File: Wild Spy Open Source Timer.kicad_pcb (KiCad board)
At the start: 2 copper layers, 30 x 31.3 mm, 16 parts, among them Q2 AO3415, Q3 AO3415, Q4 AO3415, Q5 AO3415

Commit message: PCB components placed
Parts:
- added Breakout1: CONN_02X04, MC_Footprint:4x2connnector_small, F.Cu at (212.1, 121.9)
- added C1: 0.1uF, Capacitors_SMD:C_0603_HandSoldering, B.Cu at (213.4, 104.8)
- added C2: 0.1uF, Capacitors_SMD:C_0603_HandSoldering, B.Cu at (197.5, 109.2)
- added C3: 0.1uF, Capacitors_SMD:C_0603_HandSoldering, B.Cu at (208.9, 119.4)
- added C4: 0.1uF, Capacitors_SMD:C_0603_HandSoldering, B.Cu at (199.4, 117.8)
- added C5: CL10A105KB8NNNC, Capacitors_SMD:C_0805, F.Cu at (199.3, 119.1)
- added C6: 1uF, Capacitors_SMD:C_0603_HandSoldering, B.Cu at (199.4, 121.6)
- added C8: CL10B225KQ8NFNC, Capacitors_SMD:C_0603, F.Cu at (191.1, 118.9)
- added D1: LED, LEDs:LED_0603, F.Cu at (212.7, 116.8)
- added JP1: JUMPER3, jumper:SOLDER-JUMPER_2-WAY, F.Cu at (194.9, 123.8)
- added PBus1: CONN_01X04, Pin_Headers:Pin_Header_Straight_1x04_Pitch2.54mm, F.Cu at (200.7, 97.2)
- added Q1: AO3415, MC_Footprint:SOT-23-HandSoldering, B.Cu at (195.6, 115.3)
- added Q6: AO3415, MC_Footprint:SOT-23-HandSoldering, B.Cu at (191.7, 118.8)
- added R1: 10k, Resistors_SMD:R_0603_HandSoldering, B.Cu at (208.3, 113.7)
- added R10: 3.3k, Resistors_SMD:R_0603_HandSoldering, F.Cu at (204.0, 120.7)
- added R11: 1k, Resistors_SMD:R_0603_HandSoldering, F.Cu at (212.7, 114.9)
- added R2: 10k, Resistors_SMD:R_0603_HandSoldering, B.Cu at (208.3, 115.6)
- added R3: 150k, Resistors_SMD:R_0603_HandSoldering, B.Cu at (196.4, 119.7)
- added R8: 10k, Resistors_SMD:R_0603_HandSoldering, B.Cu at (196.4, 117.8)
- added R9: 1.7k, Resistors_SMD:R_0603_HandSoldering, F.Cu at (204.0, 118.7)
- added SWD1: CONN_01X05, MC_Footprint:SWD_PROG_HEADER, F.Cu at (217.2, 120.0)
- added U1: DS3232SN, Housings_SOIC:SOIC-20W_7.5x12.8mm_Pitch1.27mm, B.Cu at (204.5, 106.0)
- added U2: TPS70933DBVR, TO_SOT_Packages_SMD:SOT-23-5_HandSoldering, F.Cu at (194.9, 118.8)
- added U3: UM6K33N, MC_Footprint:SC88(SOT363), F.Cu at (200.0, 104.8)
- added U4: UM6K33N, MC_Footprint:SC88(SOT363), F.Cu at (208.9, 104.8)
- added U5: ATSAMD21E18B, Housings_DFN_QFN:QFN-32-1EP_5x5mm_Pitch0.5mm, B.Cu at (204.1, 120.4)
- Q2, Q3, Q4, Q5: footprint TO_SOT_Packages_SMD:SOT-23 -> MC_Footprint:SOT-23-HandSoldering
- R4, R5, R6, R7: value 10k -> 100k
- moved Battery1 84.9 mm to (191.1, 122.6)
- moved CH3 66.6 mm to (191.1, 106.7)
- moved Q3 65.6 mm to (194.6, 108.6), turned to 270 degrees
- moved CH2 64.6 mm to (217.0, 97.8)
- moved Q4 60.4 mm to (213.4, 101.0)
- moved Q2 60.0 mm to (195.6, 101.0)
- moved R5 59.1 mm to (195.1, 105.4), turned to 180 degrees
- moved R6 56.9 mm to (213.4, 97.8), turned to 180 degrees
- moved CH1 56.9 mm to (191.1, 97.8)
- moved R4 54.5 mm to (195.6, 97.8), turned to 180 degrees
- moved Q5 50.3 mm to (213.4, 109.9), turned to 270 degrees
- moved CH4 48.1 mm to (217.2, 106.7)
- moved R7 43.3 mm to (213.4, 106.7), turned to 180 degrees
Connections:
- Battery1 pad 1: VAA -> /BAT+
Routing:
- net (no net): track 176.4 -> 6.88 mm, vias 6 -> 0
- net VCC: track 0.00 -> 12.0 mm
- net Net-(Q2-Pad1): track 13.0 -> 1.94 mm, vias 1 -> 0
- net +5V: track 0.00 -> 10.1 mm
- net Net-(Q3-Pad1): track 10.5 -> 2.04 mm, vias 1 -> 0
- net VAA: track 0.00 -> 8.42 mm
- net Net-(Q4-Pad1): track 10.3 -> 1.94 mm, vias 1 -> 0
- net /D+: track 0.00 -> 5.27 mm, vias 0 -> 1
- net /BAT+: track 0.00 -> 4.38 mm
- net Net-(CH2-Pad1): track 8.68 -> 4.47 mm
- net Net-(CH4-Pad1): track 8.54 -> 4.68 mm
- net Net-(Q5-Pad1): track 5.70 -> 1.97 mm
- net /D-: track 0.00 -> 3.18 mm, vias 0 -> 1
- net Net-(C6-Pad2): track 0.00 -> 2.47 mm
- net Net-(C2-Pad2): track 0.00 -> 2.42 mm
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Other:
- net class Default: clearance 0.1524 -> 0.2032; trace_width 0.1524 -> 0.2032
- rule trace_clearance: 0.1524 -> 0.2032

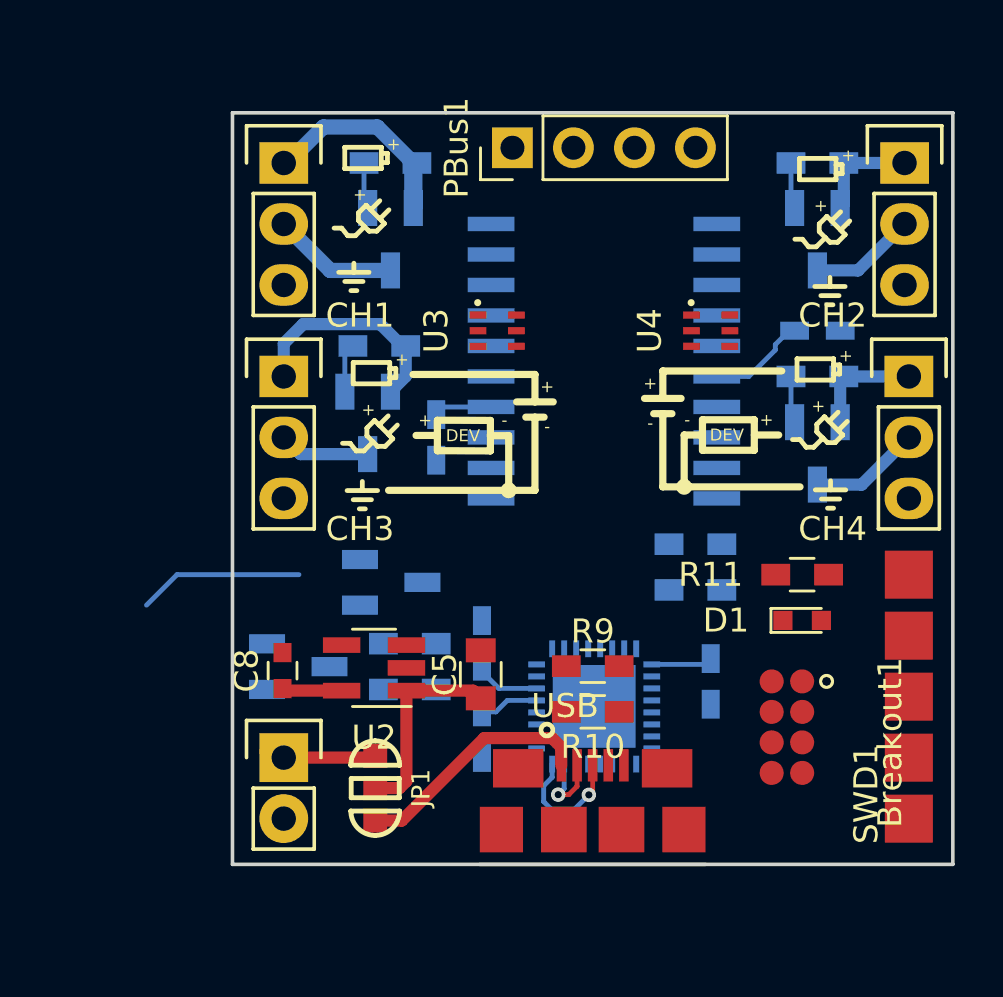
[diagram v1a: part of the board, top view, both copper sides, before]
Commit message: Routing for the Timer PCB- almost done
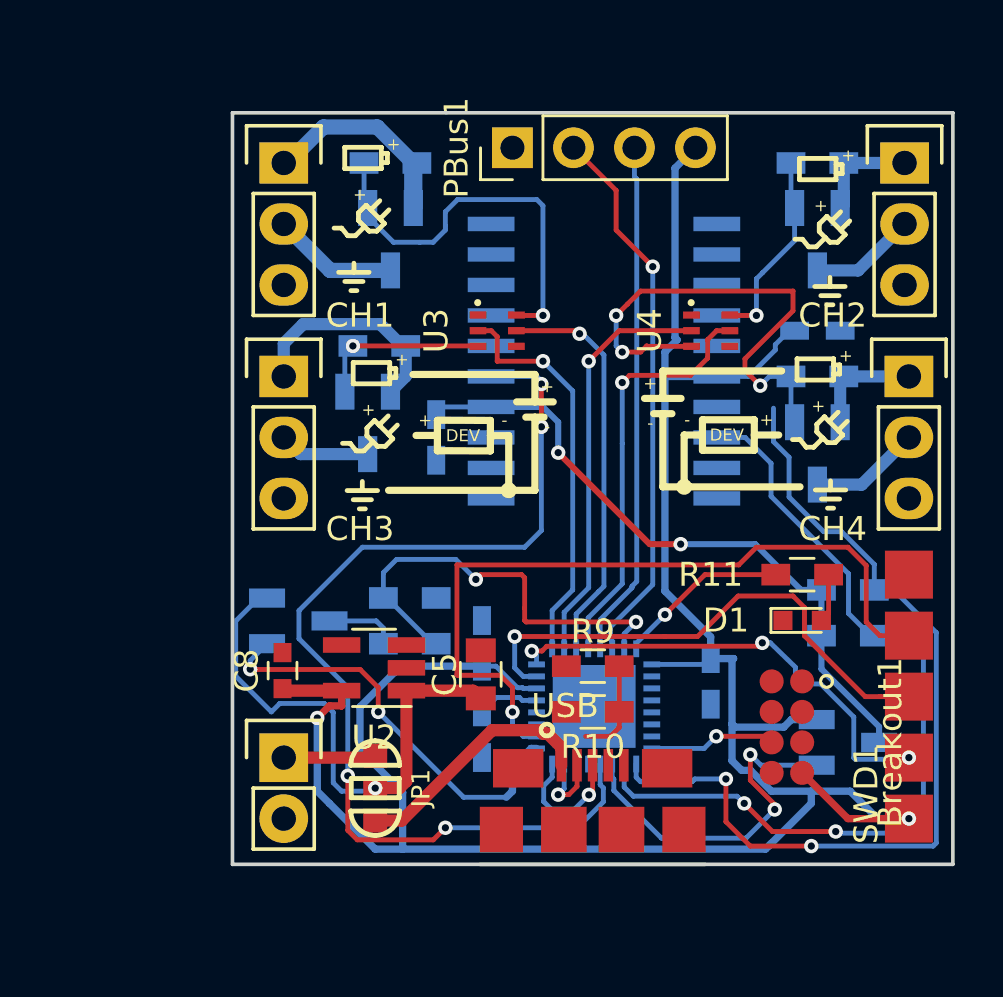
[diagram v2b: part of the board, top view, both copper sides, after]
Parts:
- moved Q1 20.2 mm to (214.6, 121.9)
- moved R2 6.63 mm to (214.6, 117.5)
- moved R1 6.63 mm to (214.6, 115.6)
- moved Q6 1.91 mm to (191.7, 116.9)
- moved R3 1.91 mm to (196.4, 117.8)
- moved R8 1.91 mm to (196.4, 115.9)
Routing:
- net VCC: track 12.0 -> 100.3 mm, vias 0 -> 2
- net /RTC_~INT: track 0.00 -> 43.0 mm, vias 0 -> 4
- net /SDA: track 0.00 -> 37.7 mm, vias 0 -> 2
- net /SCL: track 0.00 -> 35.9 mm, vias 0 -> 2
- net /NRESET: track 0.00 -> 31.9 mm, vias 0 -> 1
- net Net-(C2-Pad2): track 2.42 -> 27.4 mm, vias 0 -> 2
- net /PBus1_MRX: track 0.00 -> 23.0 mm, vias 0 -> 1
- net /SWDCLK: track 0.00 -> 21.9 mm, vias 0 -> 1
- net /PBus1_MTX: track 0.00 -> 21.5 mm
- net /SWDIO: track 0.00 -> 19.8 mm, vias 0 -> 3
- net Net-(Q5-Pad1): track 1.97 -> 20.8 mm, vias 0 -> 3
- net /VBat/15: track 0.00 -> 18.4 mm, vias 0 -> 2
- net /~BatMeasureEn: track 0.00 -> 17.5 mm, vias 0 -> 2
- net /CH4_EN: track 0.00 -> 17.5 mm, vias 0 -> 1
- net /CH2_EN: track 0.00 -> 17.3 mm, vias 0 -> 1
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
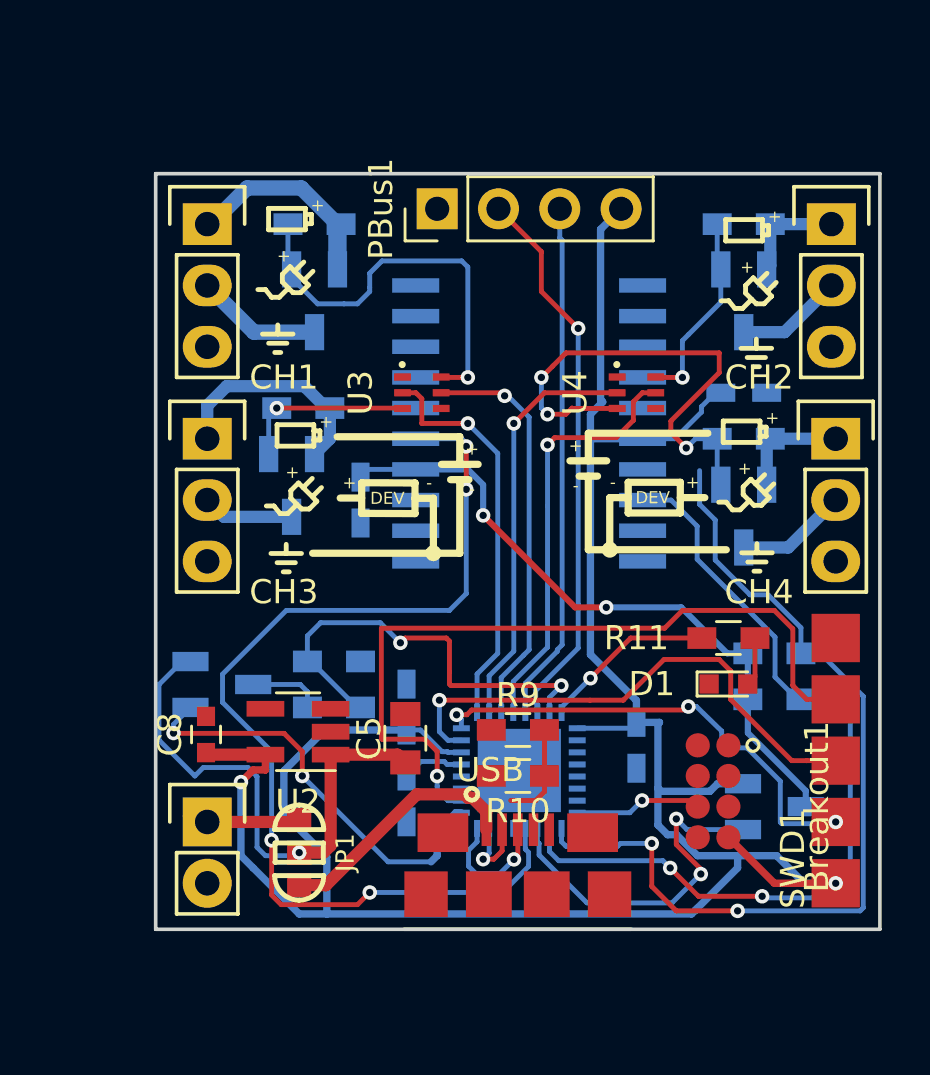
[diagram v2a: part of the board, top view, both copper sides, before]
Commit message: Cleaned up routing on PCB a bit. Made some changes to schematic, added a few things.
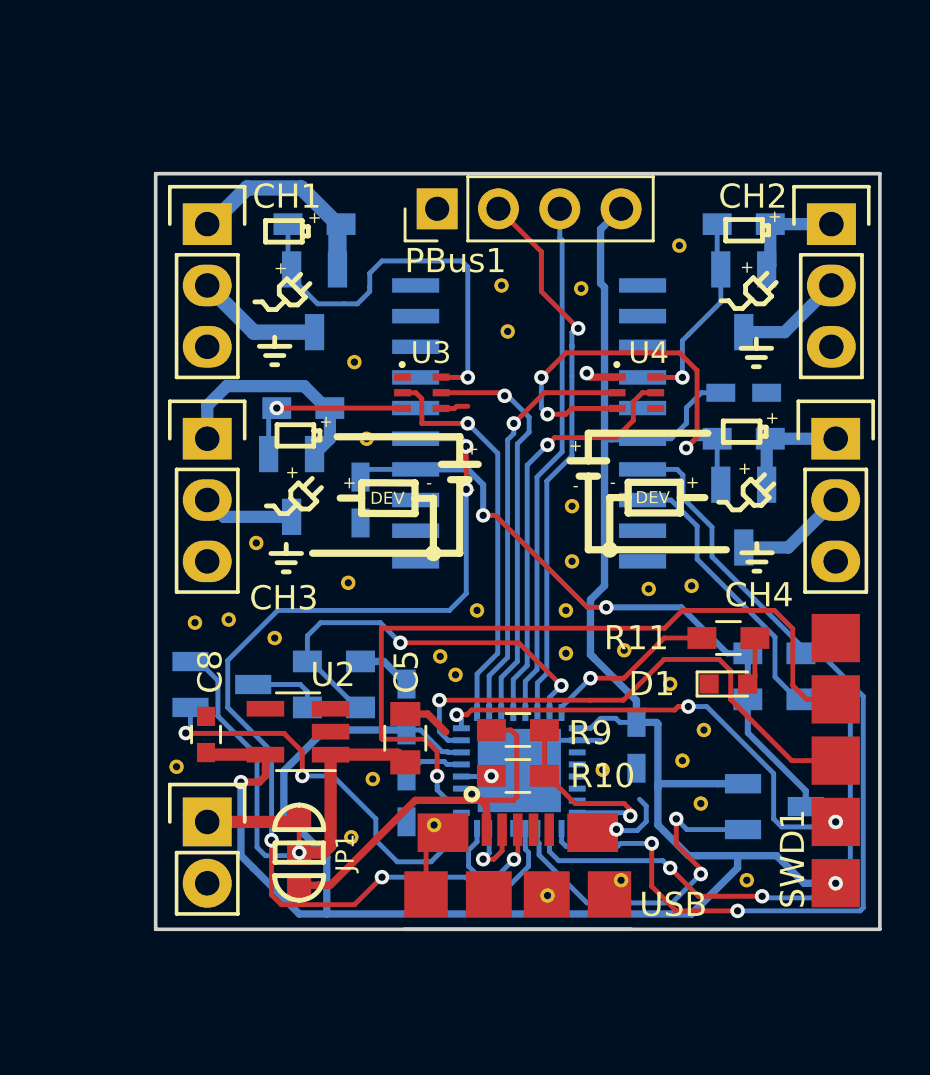
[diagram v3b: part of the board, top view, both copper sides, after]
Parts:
- removed Breakout1: CONN_02X04, MC_Footprint:4x2connnector_small
- added REF**: VIA-0.3mm, MC_Footprint:VIA-0.3mm, F.Cu at (207.5, 120.4)
- added REF**: VIA-0.3mm, MC_Footprint:VIA-0.3mm, F.Cu at (203.6, 102.2)
- added REF**: VIA-0.3mm, MC_Footprint:VIA-0.3mm, F.Cu at (206.6, 100.5)
- added REF**: VIA-0.3mm, MC_Footprint:VIA-0.3mm, F.Cu at (210.7, 98.7)
- added REF**: VIA-0.3mm, MC_Footprint:VIA-0.3mm, F.Cu at (201.4, 116.5)
- added REF**: VIA-0.3mm, MC_Footprint:VIA-0.3mm, F.Cu at (200.5, 122.7)
- added REF**: VIA-0.3mm, MC_Footprint:VIA-0.3mm, F.Cu at (205.2, 125.6)
- added REF**: VIA-0.3mm, MC_Footprint:VIA-0.3mm, F.Cu at (208.4, 115.4)
- added REF**: VIA-0.3mm, MC_Footprint:VIA-0.3mm, F.Cu at (209.4, 112.9)
- added REF**: VIA-0.3mm, MC_Footprint:VIA-0.3mm, F.Cu at (210.3, 116.8)
- added REF**: VIA-0.3mm, MC_Footprint:VIA-0.3mm, F.Cu at (213.5, 125.0)
- added REF**: VIA-0.3mm, MC_Footprint:VIA-0.3mm, F.Cu at (211.7, 118.7)
- added REF**: VIA-0.3mm, MC_Footprint:VIA-0.3mm, F.Cu at (208.3, 125.0)
- added REF**: VIA-0.3mm, MC_Footprint:VIA-0.3mm, F.Cu at (206.0, 115.6)
- added REF**: VIA-0.3mm, MC_Footprint:VIA-0.3mm, F.Cu at (189.9, 120.3)
- added REF**: VIA-0.3mm, MC_Footprint:VIA-0.3mm, F.Cu at (197.1, 123.2)
- added REF**: VIA-0.3mm, MC_Footprint:VIA-0.3mm, F.Cu at (198.0, 120.8)
- added REF**: VIA-0.3mm, MC_Footprint:VIA-0.3mm, F.Cu at (193.9, 114.9)
- added REF**: VIA-0.3mm, MC_Footprint:VIA-0.3mm, F.Cu at (192.0, 114.2)
- added REF**: VIA-0.3mm, MC_Footprint:VIA-0.3mm, F.Cu at (190.6, 114.3)
- added REF**: VIA-0.3mm, MC_Footprint:VIA-0.3mm, F.Cu at (202.3, 113.8)
- added REF**: VIA-0.3mm, MC_Footprint:VIA-0.3mm, F.Cu at (200.8, 115.7)
- added REF**: VIA-0.3mm, MC_Footprint:VIA-0.3mm, F.Cu at (210.8, 120.0)
- added REF**: VIA-0.3mm, MC_Footprint:VIA-0.3mm, F.Cu at (211.2, 112.8)
- added REF**: VIA-0.3mm, MC_Footprint:VIA-0.3mm, F.Cu at (206.2, 111.8)
- added REF**: VIA-0.3mm, MC_Footprint:VIA-0.3mm, F.Cu at (206.2, 109.5)
- added REF**: VIA-0.3mm, MC_Footprint:VIA-0.3mm, F.Cu at (197.0, 112.6)
- added REF**: VIA-0.3mm, MC_Footprint:VIA-0.3mm, F.Cu at (211.6, 121.8)
- added REF**: VIA-0.3mm, MC_Footprint:VIA-0.3mm, F.Cu at (206.0, 113.8)
- added REF**: VIA-0.3mm, MC_Footprint:VIA-0.3mm, F.Cu at (193.2, 111.0)
- added REF**: VIA-0.3mm, MC_Footprint:VIA-0.3mm, F.Cu at (197.7, 106.7)
- added REF**: VIA-0.3mm, MC_Footprint:VIA-0.3mm, F.Cu at (197.2, 103.5)
- added REF**: VIA-0.3mm, MC_Footprint:VIA-0.3mm, F.Cu at (203.3, 100.3)
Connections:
- U5 pad 15: /PA14 -> Net-(U5-Pad15)
- U5 pad 16: /PA15 -> /USBSENSE3.3
- U5 pad 22: /USBSENSE3.3 -> Net-(U5-Pad22)
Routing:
- net GND: track 0.00 -> 17.5 mm, vias 0 -> 3
- net /PA15: track 5.31 -> 0.00 mm, vias 1 -> 0
- net +5V: track 10.4 -> 15.5 mm
- net VCC: track 100.3 -> 95.5 mm
- net /USBSENSE3.3: track 4.11 -> 8.55 mm, vias 0 -> 1
- net VAA: track 22.3 -> 19.8 mm
- net Net-(Q5-Pad1): track 20.8 -> 18.6 mm
- net /VBat/15: track 18.4 -> 17.2 mm
- net (no net): track 0.00 -> 1.14 mm
- net /SDA: track 37.7 -> 38.8 mm
- added copper zone on B.Cu, net GND
- added copper zone on F.Cu, net GND

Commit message: Pretty much finished REV1 PCB. Just need to have a quick look over it and export gerbers etc.
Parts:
- removed the REF** at (207.5, 120.4)
- removed the REF** at (201.4, 116.5)
- removed the REF** at (205.2, 125.6)
- removed the REF** at (208.4, 115.4)
- removed the REF** at (209.4, 112.9)
- removed the REF** at (210.3, 116.8)
- removed the REF** at (213.5, 125.0)
- removed the REF** at (211.7, 118.7)
- removed the REF** at (208.3, 125.0)
- removed the REF** at (206.0, 115.6)
- removed the REF** at (189.9, 120.3)
- removed the REF** at (197.1, 123.2)
- removed the REF** at (198.0, 120.8)
- removed the REF** at (193.9, 114.9)
- removed the REF** at (192.0, 114.2)
- removed the REF** at (190.6, 114.3)
- removed the REF** at (202.3, 113.8)
- removed the REF** at (200.8, 115.7)
- removed the REF** at (210.8, 120.0)
- removed the REF** at (211.2, 112.8)
- removed the REF** at (211.6, 121.8)
- removed the REF** at (206.0, 113.8)
- removed the REF** at (197.2, 103.5)
- added REF**: VIA-0.3mm, MC_Footprint:VIA-0.3mm, F.Cu at (203.2, 118.6)
- added REF**: VIA-0.3mm, MC_Footprint:VIA-0.3mm, F.Cu at (190.4, 116.0)
- added REF**: VIA-0.3mm, MC_Footprint:VIA-0.3mm, F.Cu at (192.7, 116.2)
- added REF**: VIA-0.3mm, MC_Footprint:VIA-0.3mm, F.Cu at (192.5, 120.7)
- added REF**: VIA-0.3mm, MC_Footprint:VIA-0.3mm, F.Cu at (195.1, 122.8)
- added REF**: VIA-0.3mm, MC_Footprint:VIA-0.3mm, F.Cu at (197.4, 113.3)
- added REF**: VIA-0.3mm, MC_Footprint:VIA-0.3mm, F.Cu at (204.6, 104.4)
- added REF**: VIA-0.3mm, MC_Footprint:VIA-0.3mm, F.Cu at (202.7, 107.2)
- added REF**: VIA-0.3mm, MC_Footprint:VIA-0.3mm, F.Cu at (214.1, 111.2)
- added REF**: VIA-0.3mm, MC_Footprint:VIA-0.3mm, F.Cu at (214.3, 113.6)
- added REF**: VIA-0.3mm, MC_Footprint:VIA-0.3mm, F.Cu at (214.6, 115.3)
- added REF**: VIA-0.3mm, MC_Footprint:VIA-0.3mm, F.Cu at (204.8, 116.8)
- added REF**: VIA-0.3mm, MC_Footprint:VIA-0.3mm, F.Cu at (213.2, 124.5)
- added REF**: VIA-0.3mm, MC_Footprint:VIA-0.3mm, F.Cu at (215.0, 124.5)
- added REF**: VIA-0.3mm, MC_Footprint:VIA-0.3mm, F.Cu at (200.8, 114.0)
- added REF**: VIA-0.3mm, MC_Footprint:VIA-0.3mm, F.Cu at (200.5, 118.4)
- added REF**: VIA-0.3mm, MC_Footprint:VIA-0.3mm, F.Cu at (198.4, 126.3)
- added REF**: VIA-0.3mm, MC_Footprint:VIA-0.3mm, F.Cu at (192.1, 125.3)
- added REF**: VIA-0.3mm, MC_Footprint:VIA-0.3mm, F.Cu at (197.3, 124.8)
- added REF**: VIA-0.3mm, MC_Footprint:VIA-0.3mm, F.Cu at (212.0, 100.7)
- added REF**: VIA-0.3mm, MC_Footprint:VIA-0.3mm, F.Cu at (207.9, 97.4)
- added REF**: VIA-0.3mm, MC_Footprint:VIA-0.3mm, F.Cu at (192.7, 111.8)
- added SW1: SW_PUSH, OSTFootprints:KMT071NGJLHS_3x2.6mm_switch, B.Cu at (214.1, 124.6)
- added SW2: ORD213, OSTFootprints:ORD213S-1, B.Cu at (190.1, 119.7)
- C5, C8, D1, R10, R11, R9, U3, U4: moved to B.Cu
- JP1: footprint jumper:SOLDER-JUMPER_2-WAY -> OSTFootprints:SOLDER-JUMPER_2-WAY
- PBus1: footprint Pin_Headers:Pin_Header_Straight_1x04_Pitch2.54mm -> OSTFootprints:Pin_Header_Straight_1x04_Pitch2.54mm
- Q1, Q2, Q3, Q4, Q5, Q6: footprint MC_Footprint:SOT-23-HandSoldering -> OSTFootprints:SOT-23-HandSoldering
- SWD1: footprint MC_Footprint:SWD_PROG_HEADER -> OSTFootprints:SWD_PROG_HEADER_L
- U1: footprint Housings_SOIC:SOIC-20W_7.5x12.8mm_Pitch1.27mm -> OSTFootprints:SOIC-20_7.5x12.8mm_Pitch1.27mm
- U2: footprint TO_SOT_Packages_SMD:SOT-23-5_HandSoldering -> OSTFootprints:SOT-23-5_HandSoldering; moved to B.Cu
- U5: value ATSAMD21E18B -> ATSAMD21E16B; footprint Housings_DFN_QFN:QFN-32-1EP_5x5mm_Pitch0.5mm -> OSTFootprints:QFN-32-1EP_5x5mm_Pitch0.5mm
- USB1: footprint MC_Footprint:micro_USB -> OSTFootprints:micro_USB; moved to B.Cu
- moved G*** 75.8 mm to (204.2, 124.3)
- moved ? 75.8 mm to (204.2, 118.7)
- moved SWD1 27.1 mm to (190.1, 121.8), turned to 270 degrees
- moved C8 26.4 mm to (216.9, 113.4), turned to 180 degrees
- moved Battery1 26.3 mm to (217.4, 122.9)
- moved U2 22.1 mm to (216.9, 116.5), turned to 90 degrees
- moved R11 21.1 mm to (194.9, 126.2), turned to 180 degrees
- moved Q3 20.9 mm to (213.4, 99.4)
- moved Q6 20.7 mm to (212.1, 120.8), turned to 180 degrees
- moved D1 19.7 mm to (194.7, 124.8), turned to 180 degrees
- moved Q4 19.7 mm to (194.6, 107.1)
- moved Q1 19.6 mm to (195.2, 119.3), turned to 90 degrees
- moved JP1 17.7 mm to (212.6, 122.9), turned to 0 degrees
- moved C5 17.6 mm to (216.9, 120.0), turned to 180 degrees
- moved R8 15.6 mm to (212.0, 116.8)
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- renumbered CH3 to CH2, CH2 to CH3, R6 to R5, R5 to R6
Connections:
- CH2 pad 1: Net-(CH3-Pad1) -> Net-(CH2-Pad1)
- CH2 pad 2: Net-(CH3-Pad2) -> Net-(CH2-Pad2)
- CH3 pad 1: Net-(CH2-Pad1) -> Net-(CH3-Pad1)
- CH3 pad 2: Net-(CH2-Pad2) -> Net-(CH3-Pad2)
- R5 pad 1: Net-(CH2-Pad1) -> Net-(CH3-Pad1)
- R5 pad 2: Net-(Q4-Pad1) -> Net-(Q3-Pad1)
- R6 pad 1: Net-(CH3-Pad1) -> Net-(CH2-Pad1)
- R6 pad 2: Net-(Q3-Pad1) -> Net-(Q4-Pad1)
- U3 pad 3: Net-(Q3-Pad1) -> Net-(Q4-Pad1)
- U3 pad 5: /CH3_EN -> /CH2_EN
- U4 pad 2: /CH2_EN -> /CH3_EN
- U4 pad 6: Net-(Q4-Pad1) -> Net-(Q3-Pad1)
- U5 pad 14: /PA11 -> /~BatMeasureEn
- U5 pad 15: Net-(U5-Pad15) -> /BL_FW_UPDATE
- U5 pad 19: /~RTC_PEN -> /REEDSW
- U5 pad 20: /RTC_~INT -> /~RTC_PEN
- U5 pad 25: /~BatMeasureEn -> /LED
- U5 pad 7: /VBat/15 -> /RTC_~INT
- U5 pad 8: /LED -> /VBat/15
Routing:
- net /REEDSW: track 0.00 -> 28.4 mm, vias 0 -> 2
- net /RTC_~INT: track 43.2 -> 16.6 mm, vias 4 -> 2
- net VCC: track 95.5 -> 72.8 mm, vias 2 -> 6
- net /SDA: track 38.8 -> 20.0 mm
- net /NRESET: track 31.9 -> 14.5 mm
- net Net-(Q3-Pad1): track 7.26 -> 22.7 mm, vias 1 -> 4
- net /CH2_EN: track 17.3 -> 3.75 mm, vias 1 -> 0
- net Net-(C2-Pad2): track 27.4 -> 40.9 mm, vias 2 -> 3
- net /SCL: track 35.9 -> 22.8 mm
- net /CH4_EN: track 17.5 -> 4.73 mm, vias 1 -> 0
- net /CH1_EN: track 16.7 -> 3.94 mm, vias 1 -> 0
- net /CH3_EN: track 16.8 -> 4.08 mm, vias 1 -> 0
- net GND: track 17.5 -> 29.4 mm, vias 3 -> 0
- net /~BatMeasureEn: track 17.2 -> 7.53 mm, vias 2 -> 0
- net /VBat/15: track 17.2 -> 8.62 mm, vias 2 -> 0
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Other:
- board size 30 x 31.3 mm -> 30 x 32.8 mm
- net class Default: clearance 0.2032 -> 0.1524
- rule trace_clearance: 0.2032 -> 0.1524
- board text added: "BUS"
- board text added: "Channel 1"
- board text added: "Channel 2"
- board text added: "Channel 3"
- board text added: "Channel 4"
- board text added: "Frimware Update Hold Btn on Back"
- board text added: "Open Source Timer"
- board text added: "Reed Switch"
- board text added: "Rev1"
- board text added: "USB BAT"

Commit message: Finished the PCB layout
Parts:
- removed the REF** at (197.3, 124.8)
- D1: footprint LEDs:LED_0603 -> OSTFootprints:LED_0603
- U3, U4: footprint MC_Footprint:SC88(SOT363) -> OSTFootprints:SC88(SOT363)
- moved R11 1.51 mm to (195.3, 124.8)
- moved D1 1.46 mm to (195.2, 126.2)
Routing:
- net /LED: track 10.9 -> 8.67 mm
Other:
- net class Default: clearance 0.1524 -> 0.2032
- rule trace_clearance: 0.1524 -> 0.2032
- board text added: "External Sensors"
- board text added: "HBowman"
- board text added: "MCochrane"
- board text added: "Power Select"
- board text added: "STATUS"
- board text removed: "BUS"
